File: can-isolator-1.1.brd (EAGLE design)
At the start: 89.8 x 59.7 mm, 40 parts, among them IC1 MCP2562P, K1 FRS1B, Q2 BC548, Q3 BC548, Q4 BC548

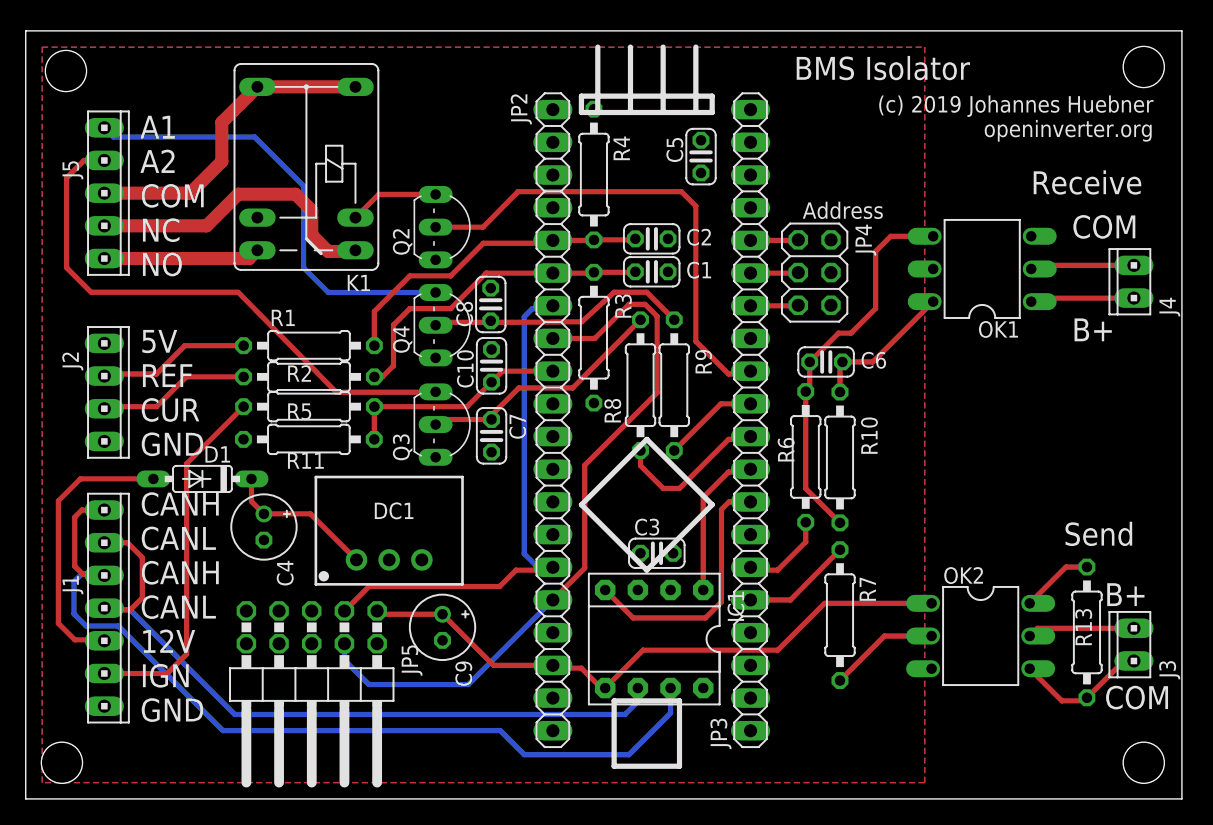
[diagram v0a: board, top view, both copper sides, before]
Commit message: Minor CAN isolator PCB mods to improve track clearance.  Added manufacturing data
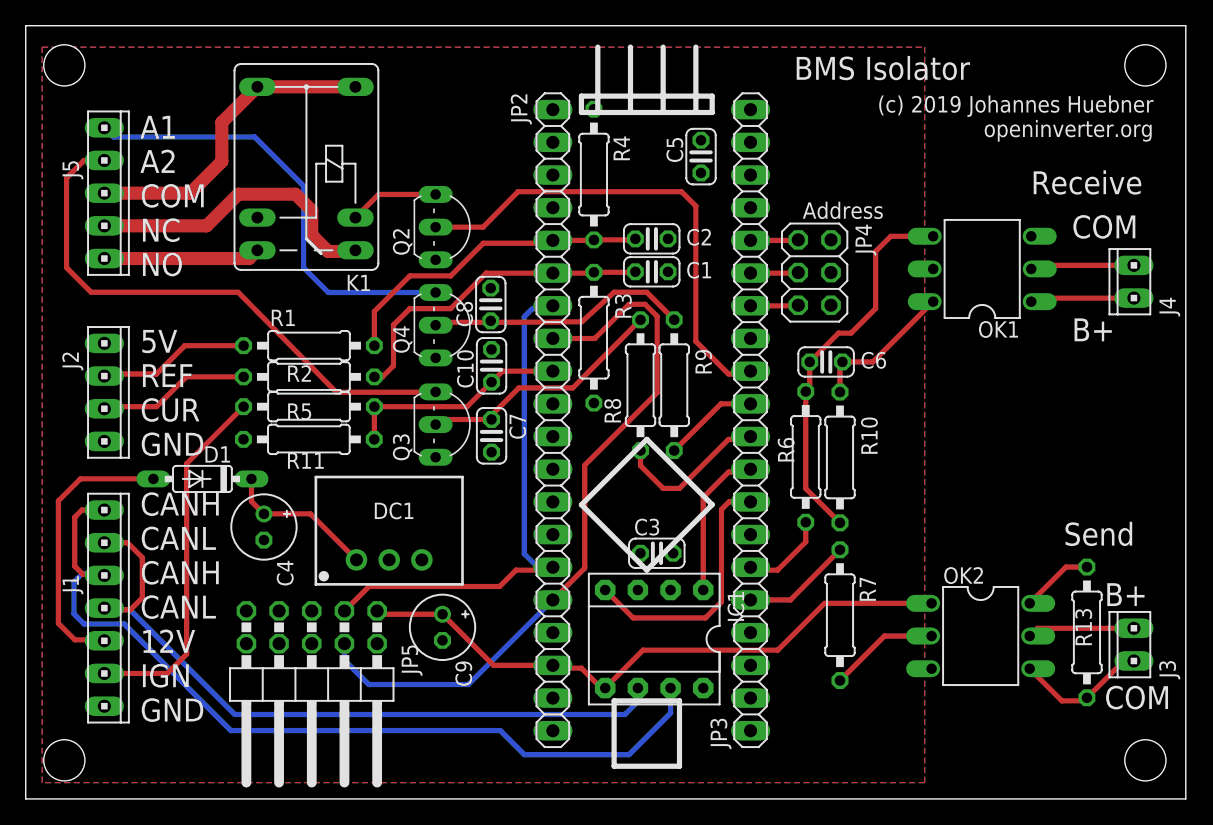
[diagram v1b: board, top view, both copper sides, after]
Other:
- board size 89.8 x 59.7 mm -> 90.1 x 60.1 mm
